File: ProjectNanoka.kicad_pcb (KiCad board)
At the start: 2 copper layers, 66 x 70 mm, 41 parts, among them K1 2-1462038-1, P1 ST_20A, Q1 2N3904BU, Q2 2N3904BU, U1 TLV70033DDCR, U2 NC7WZ16P6X, U3 PS1440P02BT

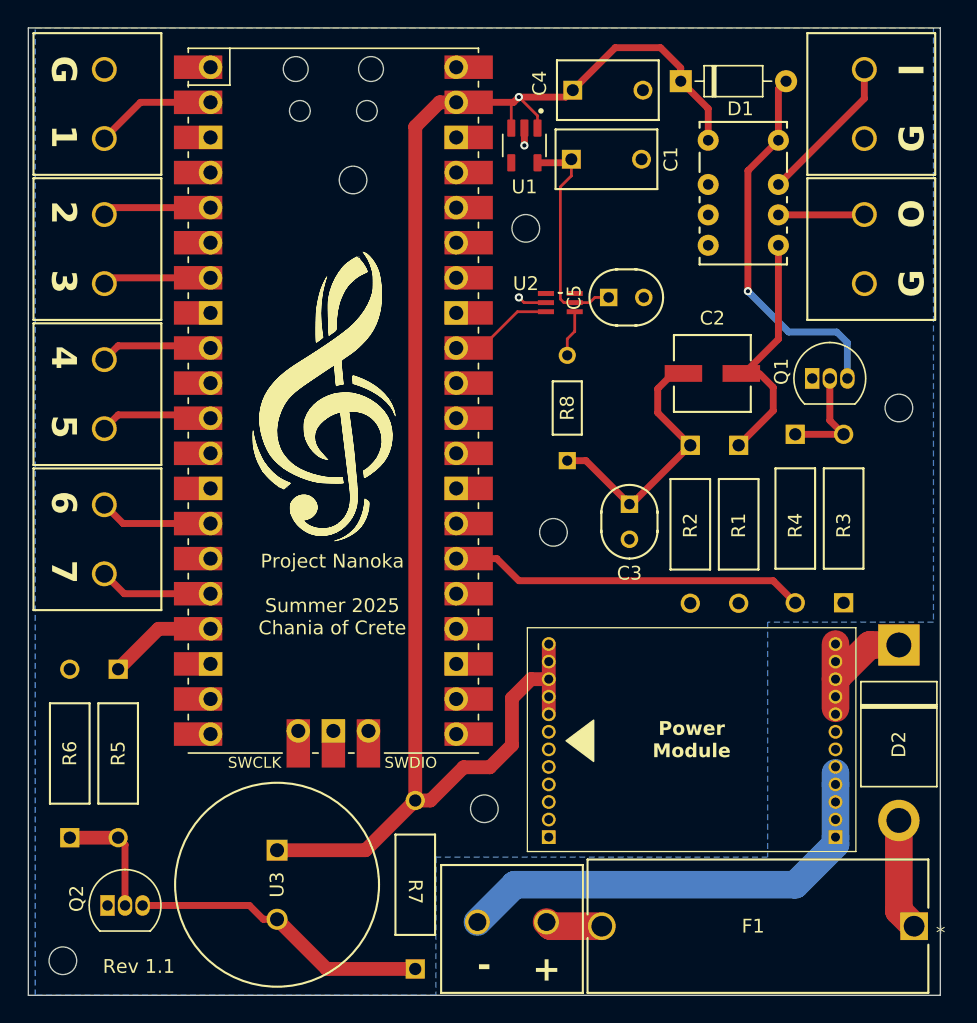
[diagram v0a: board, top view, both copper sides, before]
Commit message: Clean up the board from old components
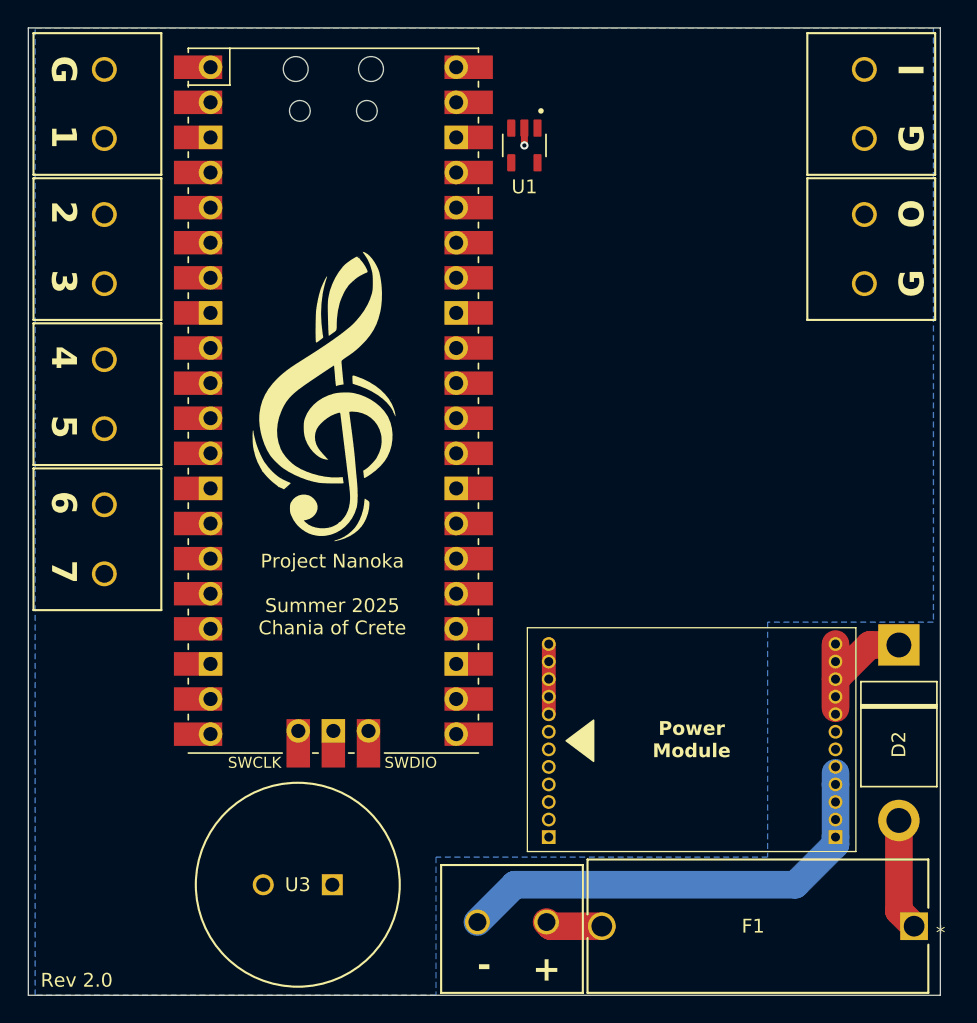
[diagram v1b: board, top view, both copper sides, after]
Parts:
- removed C1, C4: 1uf, Footprints:CAP_C330C_MR_X7R_KEM
- removed C2: 47uF, Footprints:CAP_UUQ_5X5P4_NCH
- removed C3, C5: 100nF, Footprints:CAP_C320_KEM
- removed D1: 1N4148, Footprints:D_DO-35_SOD27_P7.62mm_Horizontal
- removed the G*** at (221.0, 68.5)
- removed the G*** at (222.1, 67.7)
- removed K1: 2-1462038-1, Footprints:RELAY8-TH_NON-LATCH_1-COIL
- removed Q1, Q2: 2N3904BU, Footprints:2N3904BU
- removed R1: 1.8k, Footprints:STA_CF14_STP
- removed R2: 100, Footprints:STA_CF14_STP
- removed R3, R6: 10k, Footprints:STA_RNF14_STP
- removed R4, R5, R7: 1k, Footprints:STA_RNF14_STP
- removed R8: 220, Footprints:STA_RNMF14_STP
- removed REF** (x6): MountingHole_2mm, Footprints:MountingHole_2mm
- removed U2: NC7WZ16P6X, Footprints:SOT65P210X110-6N
- F1: value 1A -> 250mA
- moved U3 4.72 mm to (221.5, 104.0), turned to 180 degrees
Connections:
- A1 pad 11: Net-(A1-GPIO8) -> unconnected-(A1-GPIO8-Pad11)
- A1 pad 14: Net-(A1-GPIO10) -> unconnected-(A1-GPIO10-Pad14)
- A1 pad 16: Net-(A1-GPIO12) -> unconnected-(A1-GPIO12-Pad16)
- A1 pad 2: Net-(A1-GPIO1) -> unconnected-(A1-GPIO1-Pad2)
- A1 pad 26: Net-(A1-GPIO20) -> unconnected-(A1-GPIO20-Pad26)
- A1 pad 32: Net-(A1-GPIO27_ADC1) -> unconnected-(A1-GPIO27_ADC1-Pad32)
- A1 pad 5: Net-(A1-GPIO3) -> unconnected-(A1-GPIO3-Pad5)
- A1 pad 7: Net-(A1-GPIO5) -> unconnected-(A1-GPIO5-Pad7)
- A1 pad 9: Net-(A1-GPIO6) -> unconnected-(A1-GPIO6-Pad9)
- A_IN1 pad 2: AIN -> unconnected-(A_IN1-Pin_2-Pad2)
- A_OUT1 pad 1: GNDPWR -> unconnected-(A_OUT1-Pin_1-Pad1)
- A_OUT1 pad 2: AOUT -> unconnected-(A_OUT1-Pin_2-Pad2)
- GT1 pad 1: GNDPWR -> unconnected-(GT1-Pin_1-Pad1)
- GT1 pad 2: Net-(A1-GPIO1) -> GNDPWR
- GT2 pad 1: Net-(A1-GPIO3) -> unconnected-(GT2-Pin_1-Pad1)
- GT2 pad 2: Net-(A1-GPIO5) -> unconnected-(GT2-Pin_2-Pad2)
- GT3 pad 1: Net-(A1-GPIO6) -> unconnected-(GT3-Pin_1-Pad1)
- GT3 pad 2: Net-(A1-GPIO8) -> unconnected-(GT3-Pin_2-Pad2)
- GT4 pad 1: Net-(A1-GPIO10) -> unconnected-(GT4-Pin_1-Pad1)
- GT4 pad 2: Net-(A1-GPIO12) -> unconnected-(GT4-Pin_2-Pad2)
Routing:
- net +5V: track 114.4 -> 5.08 mm, vias 1 -> 0
- net Net-(D1-A): track 27.7 -> 0.00 mm, vias 1 -> 0
- net Net-(A1-GPIO20): track 25.9 -> 0.00 mm
- net Net-(Q2-PadC): track 21.6 -> 0.00 mm
- net Net-(C2-Pad1): track 18.6 -> 0.00 mm
- net PWM: track 17.2 -> 0.00 mm
- net 3.3AS: track 16.8 -> 0.00 mm
- net AIN: track 10.9 -> 0.00 mm
- net Net-(A1-GPIO1): track 8.77 -> 0.00 mm
- net Net-(Q2-PadB): track 8.61 -> 0.00 mm
- net Net-(A1-GPIO10): track 8.45 -> 0.00 mm
- net Net-(A1-GPIO12): track 8.37 -> 0.00 mm
- net Net-(Q1-PadB): track 8.34 -> 0.00 mm
- net Net-(A1-GPIO8): track 8.20 -> 0.00 mm
- net Net-(A1-GPIO6): track 8.17 -> 0.00 mm
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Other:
- board text added: "Rev 2.0"
- board text removed: "Pull down resistors required"
- board text removed: "Rev 1.1"

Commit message: Update board with new layout and schematic
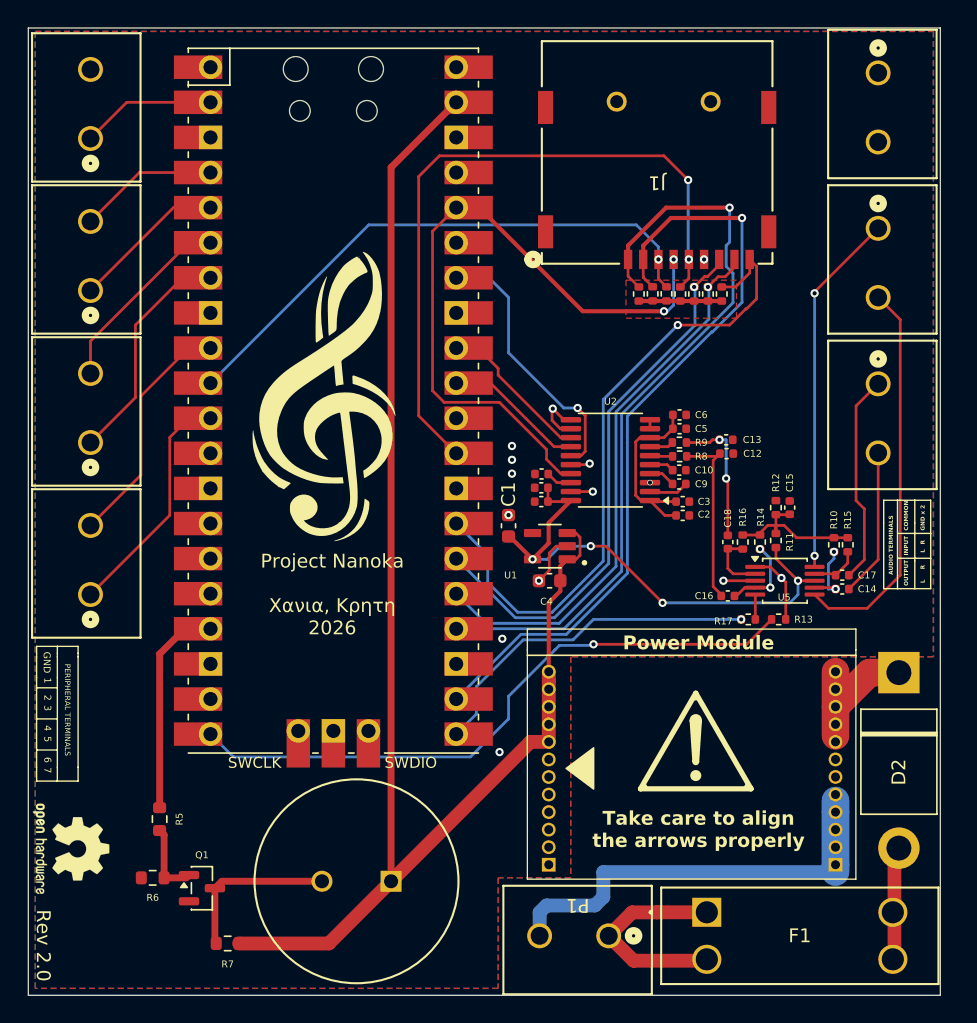
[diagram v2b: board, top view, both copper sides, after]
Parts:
- added A_GND1: TERM, NewFootprints:TERMINAL, F.Cu at (261.0, 45.2)
- added C1: 1uf, Capacitor_SMD:C_0603_1608Metric, F.Cu at (234.2, 78.0)
- added C10: 2.2u, Capacitor_SMD:C_0402_1005Metric, F.Cu at (246.6, 74.0)
- added C11: 100n, Capacitor_SMD:C_0402_1005Metric, F.Cu at (236.6, 74.3)
- added C12: 2.2n, Capacitor_SMD:C_0402_1005Metric, F.Cu at (250.0, 72.8)
- added C13: 2.2n, Capacitor_SMD:C_0402_1005Metric, F.Cu at (250.0, 71.8)
- added C14: 4.7uF, Capacitor_SMD:C_0402_1005Metric, F.Cu at (258.4, 82.6)
- added C15: 1uF, Capacitor_SMD:C_0402_1005Metric, F.Cu at (254.6, 76.7)
- added C16: 4.7uF, Capacitor_SMD:C_0402_1005Metric, F.Cu at (250.1, 83.1)
- added C17: 4.7uF, Capacitor_SMD:C_0402_1005Metric, F.Cu at (258.4, 81.6)
- added C18: 4.7uF, Capacitor_SMD:C_0402_1005Metric, F.Cu at (250.1, 79.2)
- added C2: 10u, Capacitor_SMD:C_0402_1005Metric, F.Cu at (246.9, 77.3)
- added C3: 100n, Capacitor_SMD:C_0402_1005Metric, F.Cu at (246.9, 76.3)
- added C4: 1uf, Capacitor_SMD:C_0603_1608Metric, F.Cu at (237.2, 82.0)
- added C5: 100n, Capacitor_SMD:C_0402_1005Metric, F.Cu at (246.6, 71.0)
- added C6: 10u, Capacitor_SMD:C_0402_1005Metric, F.Cu at (246.6, 70.0)
- added C7: 100n, Capacitor_SMD:C_0402_1005Metric, F.Cu at (236.6, 75.3)
- added C8: 10u, Capacitor_SMD:C_0402_1005Metric, F.Cu at (236.6, 76.3)
- added C9: 2.2u, Capacitor_SMD:C_0402_1005Metric, F.Cu at (246.6, 75.0)
- added J1: SD_SLOT, NewFootprints:SD_SLOT, F.Cu at (245.0, 51.0)
- added Q1: MMBT3904, Package_TO_SOT_SMD:SOT-23, F.Cu at (212.1, 104.2)
- added R10: 100k, Resistor_SMD:R_0402_1005Metric, F.Cu at (257.8, 79.4)
- added R11: 250k, Resistor_SMD:R_0402_1005Metric, F.Cu at (253.6, 79.1)
- added R12: 250k, Resistor_SMD:R_0402_1005Metric, F.Cu at (253.6, 76.7)
- added R13: 2k, Resistor_SMD:R_0402_1005Metric, F.Cu at (253.8, 84.8)
- added R14: 100k, Resistor_SMD:R_0402_1005Metric, F.Cu at (252.4, 79.2)
- added R15: 100k, Resistor_SMD:R_0402_1005Metric, F.Cu at (258.8, 79.4)
- added R16: 100k, Resistor_SMD:R_0402_1005Metric, F.Cu at (251.2, 79.2)
- added R17: 2k, Resistor_SMD:R_0402_1005Metric, F.Cu at (251.6, 84.8)
- added R18: 47k, Resistor_SMD:R_0402_1005Metric, F.Cu at (245.7, 61.2)
- added R19: 47k, Resistor_SMD:R_0402_1005Metric, F.Cu at (243.7, 61.2)
- added R20: 47k, Resistor_SMD:R_0402_1005Metric, F.Cu at (244.7, 61.2)
- added R21: 47k, Resistor_SMD:R_0402_1005Metric, F.Cu at (247.7, 61.2)
- added R22: 47k, Resistor_SMD:R_0402_1005Metric, F.Cu at (249.7, 61.2)
- added R23: 47k, Resistor_SMD:R_0402_1005Metric, F.Cu at (246.7, 61.2)
- added R24: 47k, Resistor_SMD:R_0402_1005Metric, F.Cu at (248.7, 61.2)
- added R5: 1k, Resistor_SMD:R_0603_1608Metric, F.Cu at (209.0, 99.2)
- added R6: 10k, Resistor_SMD:R_0603_1608Metric, F.Cu at (208.5, 103.5)
- added R7: 1k, Resistor_SMD:R_0603_1608Metric, F.Cu at (213.9, 108.2)
- added R8: 270, Resistor_SMD:R_0402_1005Metric, F.Cu at (246.6, 73.0)
- added R9: 270, Resistor_SMD:R_0402_1005Metric, F.Cu at (246.6, 72.0)
- added REF**: Symbol_Attention_Triangle_8x7mm_Copper, Symbol:Symbol_Attention_Triangle_8x7mm_Copper, F.Cu at (247.8, 93.6)
- added REF**: OSHW-Logo2_7.3x6mm_SilkScreen, Symbol:OSHW-Logo2_7.3x6mm_SilkScreen, F.Cu at (202.6, 101.4)
- added U2: PCM5101A, Package_SO:TSSOP-20_4.4x6.5mm_P0.65mm, F.Cu at (241.6, 73.3)
- added U5: TS5A23159DGS, Package_SO:TSSOP-10_3x3mm_P0.5mm, F.Cu at (254.2, 82.0)
- A_IN1, A_OUT1, GT1, GT2, GT3, GT4, P1: value ST_20A -> TERM; footprint Footprints:CONN_1935161_PXC -> NewFootprints:TERMINAL
- F1: value 250mA -> 1A; footprint Footprints:20x300_FUSE_HOLDER_0PTF0078P_LTF -> NewFootprints:FUSE_HOLDER
- moved U1 29.1 mm to (237.2, 79.5), turned to 180 degrees
- moved A_IN1 17.8 mm to (261.0, 67.8), turned to -90 degrees
- moved F1 15.0 mm to (248.6, 106.0), turned to 0 degrees
- moved P1 9.55 mm to (241.5, 107.7), turned to 180 degrees
- moved GT4 6.58 mm to (204.0, 83.0), turned to 90 degrees
- moved GT3 6.08 mm to (204.0, 72.0), turned to 90 degrees
- moved GT2 5.59 mm to (204.0, 61.0), turned to 90 degrees
- moved GT1 5.10 mm to (204.0, 50.0), turned to 90 degrees
- moved U3 4.26 mm to (225.8, 103.8)
- moved A_OUT1 4.12 mm to (261.0, 56.5), turned to -90 degrees
- moved D2 2.00 mm to (262.5, 88.7)
- moved H1 2.00 mm to (238.7, 103.6)
- moved H2 2.00 mm to (259.4, 103.6)
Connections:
- A1 pad 10: unconnected-(A1-GPIO7-Pad10) -> SD_CMD
- A1 pad 11: unconnected-(A1-GPIO8-Pad11) -> GP7
- A1 pad 2: unconnected-(A1-GPIO1-Pad2) -> GP1
- A1 pad 20: unconnected-(A1-GPIO15-Pad20) -> GPIO15
- A1 pad 21: unconnected-(A1-GPIO16-Pad21) -> GPIO16
- A1 pad 22: unconnected-(A1-GPIO17-Pad22) -> SD_CD/DAT3
- A1 pad 24: unconnected-(A1-GPIO18-Pad24) -> SD_DAT2
- A1 pad 25: unconnected-(A1-GPIO19-Pad25) -> SD_DAT1
- A1 pad 26: unconnected-(A1-GPIO20-Pad26) -> SD_DAT0
- A1 pad 27: unconnected-(A1-GPIO21-Pad27) -> SD_CD
- A1 pad 29: unconnected-(A1-GPIO22-Pad29) -> SD_CLK
- A1 pad 31: unconnected-(A1-GPIO26_ADC0-Pad31) -> GPIO26
- A1 pad 32: unconnected-(A1-GPIO27_ADC1-Pad32) -> GPIO27
- A1 pad 33: unconnected-(A1-AGND-Pad33) -> GNDPWR
- A1 pad 34: unconnected-(A1-GPIO28_ADC2-Pad34) -> GPIO28
- A1 pad 36: unconnected-(A1-3V3-Pad36) -> 3V3
- A1 pad 4: unconnected-(A1-GPIO2-Pad4) -> GP2
- A1 pad 5: unconnected-(A1-GPIO3-Pad5) -> GP3
- A1 pad 6: unconnected-(A1-GPIO4-Pad6) -> GP4
- A1 pad 7: unconnected-(A1-GPIO5-Pad7) -> GP5
- A1 pad 9: unconnected-(A1-GPIO6-Pad9) -> GP6
- A_IN1 pad 1: GNDPWR -> EXT_AUDIO_RIGHT
- A_IN1 pad 2: unconnected-(A_IN1-Pin_2-Pad2) -> EXT_AUDIO_LEFT
- A_OUT1 pad 1: unconnected-(A_OUT1-Pin_1-Pad1) -> AUDIO_OUT_RIGHT
- A_OUT1 pad 2: unconnected-(A_OUT1-Pin_2-Pad2) -> AUDIO_OUT_LEFT
- F1 pad 1: Net-(D2-A) -> Net-(P1-Pin_1)
- F1 pad 2: Net-(P1-Pin_2) -> Net-(P1-Pin_1)
- GT1 pad 1: unconnected-(GT1-Pin_1-Pad1) -> GP1
- GT2 pad 1: unconnected-(GT2-Pin_1-Pad1) -> GP3
- GT2 pad 2: unconnected-(GT2-Pin_2-Pad2) -> GP2
- GT3 pad 1: unconnected-(GT3-Pin_1-Pad1) -> GP5
- GT3 pad 2: unconnected-(GT3-Pin_2-Pad2) -> GP4
- GT4 pad 1: unconnected-(GT4-Pin_1-Pad1) -> GP7
- GT4 pad 2: unconnected-(GT4-Pin_2-Pad2) -> GP6
- P1 pad 1: Net-(H2-Pin_1) -> Net-(P1-Pin_1)
- P1 pad 2: Net-(P1-Pin_2) -> Net-(H2-Pin_1)
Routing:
- net +5V: track 5.08 -> 106.1 mm
- net 3V3: track 0.00 -> 68.6 mm, vias 0 -> 2
- net SD_CD/DAT3: track 0.00 -> 56.4 mm, vias 0 -> 1
- net SD_DAT2: track 0.00 -> 55.5 mm, vias 0 -> 1
- net SD_CLK: track 0.00 -> 50.0 mm, vias 0 -> 2
- net SD_CD: track 0.00 -> 48.3 mm, vias 0 -> 1
- net GPIO15: track 0.00 -> 46.4 mm, vias 0 -> 1
- net SD_CMD: track 0.00 -> 40.9 mm, vias 0 -> 1
- net SD_DAT1: track 0.00 -> 40.0 mm, vias 0 -> 1
- net SD_DAT0: track 0.00 -> 39.6 mm, vias 0 -> 1
- net 3.3AS: track 0.00 -> 37.3 mm, vias 0 -> 4
- net AUDIO_OUT_LEFT: track 0.00 -> 28.4 mm
- net AUDIO_OUT_RIGHT: track 0.00 -> 26.3 mm, vias 0 -> 2
- net GPIO16: track 0.00 -> 25.2 mm, vias 0 -> 1
- net GPIO28: track 0.00 -> 19.6 mm, vias 0 -> 1
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- added copper zone on F.Cu, net 3V3
- added copper zone on F.Cu, net GNDPWR
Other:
- board text added: "AUDIO TERMINALS"
- board text added: "COMMON"
- board text added: "GND"
- board text added: "GND x 2"
- board text added: "INPUT"
- board text added: "L"
- board text added: "OUTPUT"
- board text added: "PERIPHERAL TERMINALS"
- board text added: "Project Nanoka"
- board text added: "Project Nanoka Χανια, Κρητη 2026"
- board text added: "R"
- board text added: "Take care to align the arrows properly"
- board text removed: "+"
- board text removed: "-"
- board text removed: "G"
- board text removed: "I"
- board text removed: "O"
- board text removed: "Project Nanoka Summer 2025 Chania of Crete"
